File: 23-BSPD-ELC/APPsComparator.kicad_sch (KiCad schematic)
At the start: 22 parts, among them U14 LM339, U15 LM239

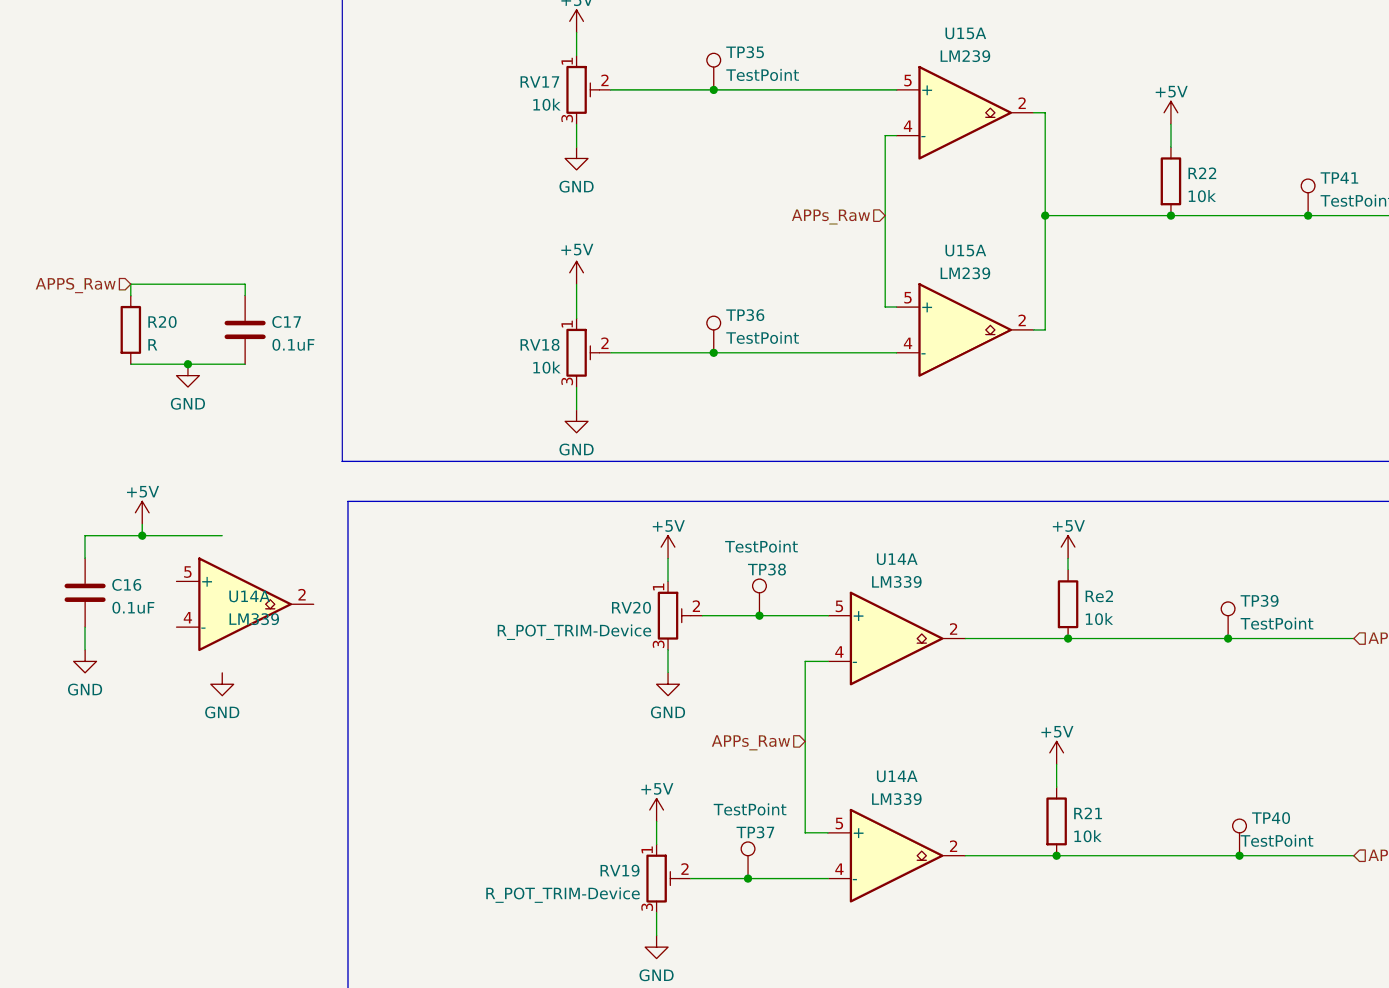
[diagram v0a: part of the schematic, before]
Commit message: Revision changes and updates to some footprints
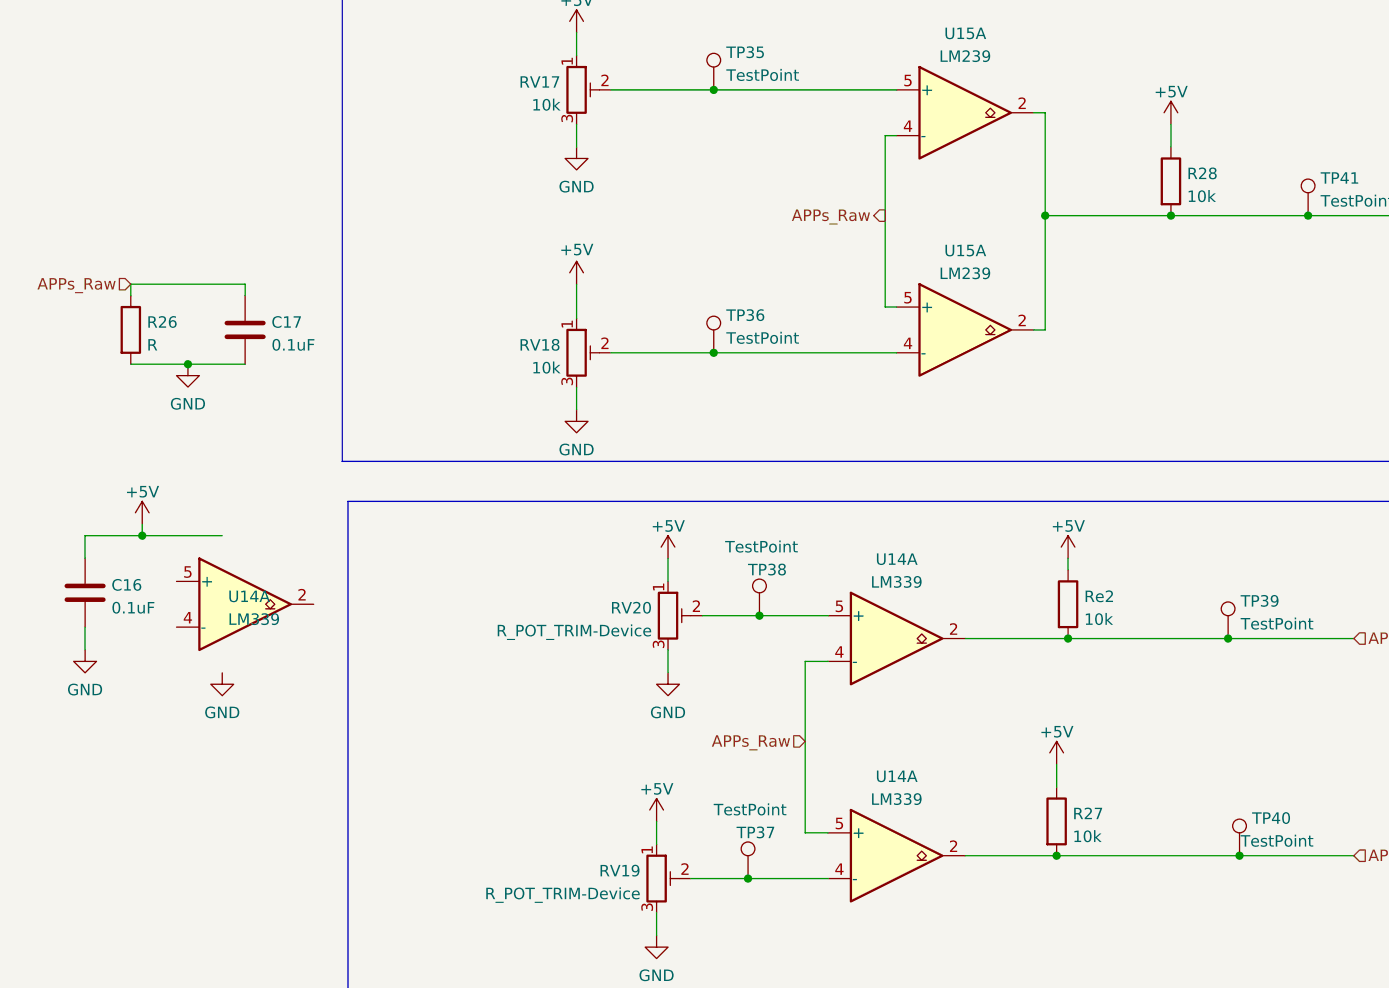
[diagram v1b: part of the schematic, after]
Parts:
- renumbered R20 to R26, R21 to R27, R22 to R28
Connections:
- net APPS_Raw is gone; now on net APPs_Raw: C17.1, R26.1
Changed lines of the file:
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@@
     (effects (font (size 1.27 1.27)) (justify left))
   )
-  (hierarchical_label "APPS_Raw" (shape input) (at 34.29 54.61 180)
+  (hierarchical_label "APPs_Raw" (shape input) (at 34.29 54.61 180)
     (effects (font (size 1.27 1.27)) (justify right))
   )
@@
     (effects (font (size 1.27 1.27)) (justify left))
   )
-  (hierarchical_label "APPs_Raw" (shape input) (at 118.11 46.99 180)
+  (hierarchical_label "APPs_Raw" (shape output) (at 118.11 46.99 180)
     (effects (font (size 1.27 1.27)) (justify right))
   )
@@
   (symbol (lib_id "power:+5V") (at 92.71 114.3 0)
     (in_bom yes) (on_board yes) (fields_autoplaced)
-    (property "Reference" "#PWR0102" (id 0) (at 92.71 118.11 0)
+    (property "Reference" "#PWR0108" (id 0) (at 92.71 118.11 0)
       (effects (font (size 1.27 1.27)) hide)
     )
@@
   (symbol (lib_id "power:GND") (at 93.98 97.79 0)
     (in_bom yes) (on_board yes) (fields_autoplaced)
-    (property "Reference" "#PWR0105" (id 0) (at 93.98 104.14 0)
+    (property "Reference" "#PWR0111" (id 0) (at 93.98 104.14 0)
       (effects (font (size 1.27 1.27)) hide)
     )
@@
   (symbol (lib_id "power:+5V") (at 83.82 54.61 0)
     (in_bom yes) (on_board yes)
-    (property "Reference" "#PWR0100" (id 0) (at 83.82 58.42 0)
+    (property "Reference" "#PWR0106" (id 0) (at 83.82 58.42 0)
       (effects (font (size 1.27 1.27)) hide)
     )
@@
   (symbol (lib_id "Device:R") (at 149.86 43.18 0)
     (in_bom yes) (on_board yes) (fields_autoplaced)
-    (property "Reference" "R22" (id 0) (at 151.638 42.3453 0)
+    (property "Reference" "R28" (id 0) (at 151.638 42.3453 0)
       (effects (font (size 1.27 1.27)) (justify left))
     )
@@
   (symbol (lib_id "power:GND") (at 29.21 95.25 0)
     (in_bom yes) (on_board yes) (fields_autoplaced)
-    (property "Reference" "#PWR094" (id 0) (at 29.21 101.6 0)
+    (property "Reference" "#PWR0100" (id 0) (at 29.21 101.6 0)
       (effects (font (size 1.27 1.27)) hide)
     )
@@
   (symbol (lib_id "power:+5V") (at 149.86 36.83 0)
     (in_bom yes) (on_board yes) (fields_autoplaced)
-    (property "Reference" "#PWR0108" (id 0) (at 149.86 40.64 0)
+    (property "Reference" "#PWR0114" (id 0) (at 149.86 40.64 0)
       (effects (font (size 1.27 1.27)) hide)
     )
@@
   (symbol (lib_id "power:+5V") (at 138.43 85.09 0)
     (in_bom yes) (on_board yes) (fields_autoplaced)
-    (property "Reference" "#PWR0107" (id 0) (at 138.43 88.9 0)
+    (property "Reference" "#PWR0113" (id 0) (at 138.43 88.9 0)
       (effects (font (size 1.27 1.27)) hide)
     )
@@
   (symbol (lib_id "power:+5V") (at 83.82 26.67 0)
     (in_bom yes) (on_board yes) (fields_autoplaced)
-    (property "Reference" "#PWR098" (id 0) (at 83.82 30.48 0)
+    (property "Reference" "#PWR0104" (id 0) (at 83.82 30.48 0)
       (effects (font (size 1.27 1.27)) hide)
     )
@@
   (symbol (lib_id "power:GND") (at 83.82 39.37 0)
     (in_bom yes) (on_board yes) (fields_autoplaced)
-    (property "Reference" "#PWR099" (id 0) (at 83.82 45.72 0)
+    (property "Reference" "#PWR0105" (id 0) (at 83.82 45.72 0)
       (effects (font (size 1.27 1.27)) hide)
     )
@@
   (symbol (lib_id "Device:R") (at 137.16 114.3 0)
     (in_bom yes) (on_board yes) (fields_autoplaced)
-    (property "Reference" "R21" (id 0) (at 138.938 113.4653 0)
+    (property "Reference" "R27" (id 0) (at 138.938 113.4653 0)
       (effects (font (size 1.27 1.27)) (justify left))
     )
@@
   (symbol (lib_id "power:GND") (at 44.45 97.79 0)
     (in_bom yes) (on_board yes) (fields_autoplaced)
-    (property "Reference" "#PWR097" (id 0) (at 44.45 104.14 0)
+    (property "Reference" "#PWR0103" (id 0) (at 44.45 104.14 0)
       (effects (font (size 1.27 1.27)) hide)
     )
@@
   (symbol (lib_id "power:GND") (at 40.64 63.5 0)
     (in_bom yes) (on_board yes) (fields_autoplaced)
-    (property "Reference" "#PWR096" (id 0) (at 40.64 69.85 0)
+    (property "Reference" "#PWR0102" (id 0) (at 40.64 69.85 0)
       (effects (font (size 1.27 1.27)) hide)
     )
@@
   (symbol (lib_id "power:+5V") (at 93.98 85.09 0)
     (in_bom yes) (on_board yes) (fields_autoplaced)
-    (property "Reference" "#PWR0104" (id 0) (at 93.98 88.9 0)
+    (property "Reference" "#PWR0110" (id 0) (at 93.98 88.9 0)
       (effects (font (size 1.27 1.27)) hide)
     )
@@
   (symbol (lib_id "power:+5V") (at 35.56 81.28 0)
     (in_bom yes) (on_board yes) (fields_autoplaced)
-    (property "Reference" "#PWR095" (id 0) (at 35.56 85.09 0)
+    (property "Reference" "#PWR0101" (id 0) (at 35.56 85.09 0)
       (effects (font (size 1.27 1.27)) hide)
     )
@@
   (symbol (lib_id "power:+5V") (at 137.16 107.95 0)
     (in_bom yes) (on_board yes) (fields_autoplaced)
-    (property "Reference" "#PWR0106" (id 0) (at 137.16 111.76 0)
+    (property "Reference" "#PWR0112" (id 0) (at 137.16 111.76 0)
       (effects (font (size 1.27 1.27)) hide)
     )
@@
   (symbol (lib_id "power:GND") (at 83.82 68.58 0)
     (in_bom yes) (on_board yes) (fields_autoplaced)
-    (property "Reference" "#PWR0101" (id 0) (at 83.82 74.93 0)
+    (property "Reference" "#PWR0107" (id 0) (at 83.82 74.93 0)
       (effects (font (size 1.27 1.27)) hide)
     )
@@
   (symbol (lib_id "Device:R") (at 34.29 59.69 0)
     (in_bom yes) (on_board yes) (fields_autoplaced)
-    (property "Reference" "R20" (id 0) (at 36.068 58.8553 0)
+    (property "Reference" "R26" (id 0) (at 36.068 58.8553 0)
       (effects (font (size 1.27 1.27)) (justify left))
     )
@@
   (symbol (lib_id "power:GND") (at 92.71 127 0)
     (in_bom yes) (on_board yes) (fields_autoplaced)
-    (property "Reference" "#PWR0103" (id 0) (at 92.71 133.35 0)
-      (effects (font (size 1.27 1.27)) hide)
-    )
+    (property "Reference" "#PWR0109" (id 0) (at 92.71 133.35 0)
+      (effects (font (size 1.27 1.27)) hide)
+    )

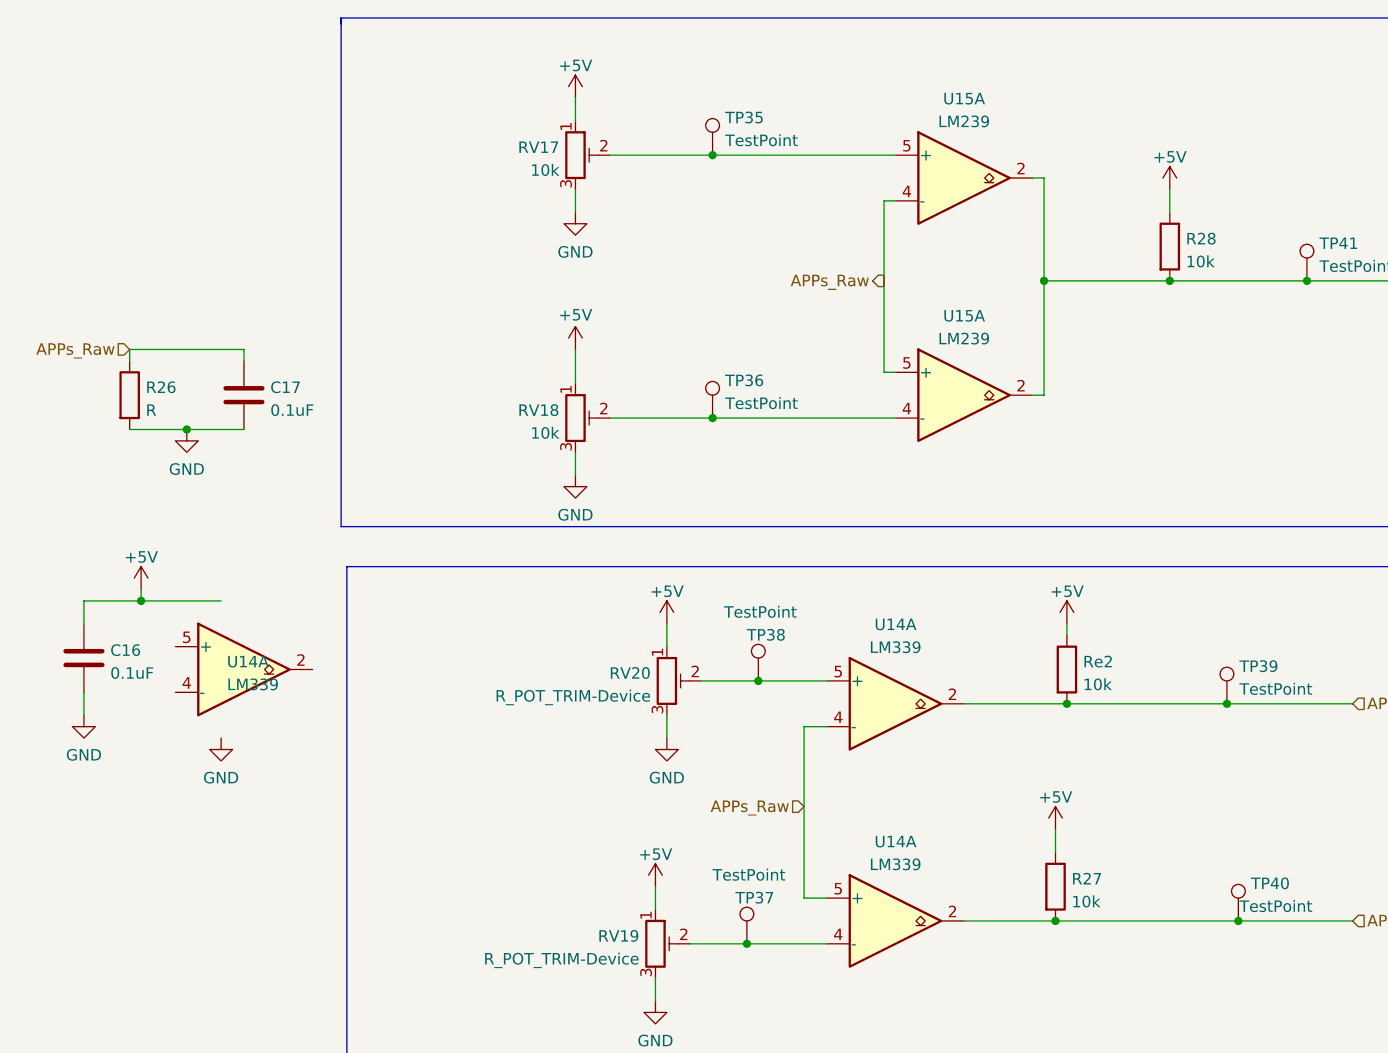
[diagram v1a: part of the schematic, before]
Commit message: Updated pcb layout; Watchdog on board still in progress
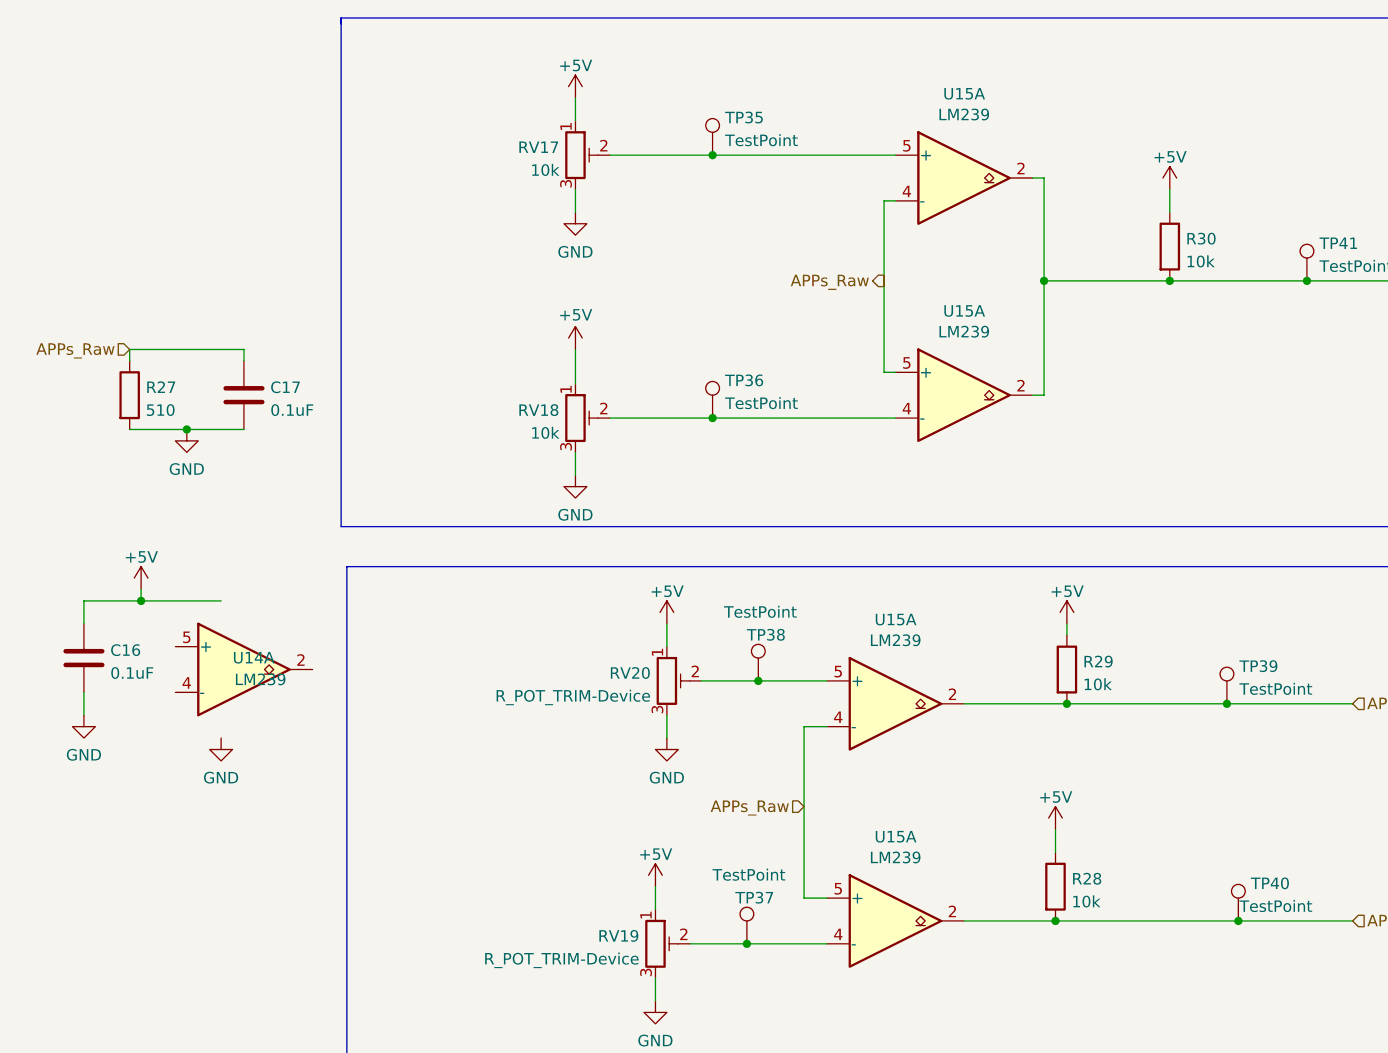
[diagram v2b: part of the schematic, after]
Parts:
- removed U14 (x3): LM339, symbol Comparator:LM339
- removed U15 (x2): LM239, symbol Comparator:LM339
- added U14: LM239, Package_SO:SO-14_3.9x8.65mm_P1.27mm, symbol Comparator:LM339
- added U15 (x4): LM239, Package_SO:SO-14_3.9x8.65mm_P1.27mm, symbol Comparator:LM2901
- R27: renamed from R26; value R -> 510
- R29: renamed from Re2; footprint (none) -> Resistor_SMD:R_0603_1608Metric_Pad0.98x0.95mm_HandSolder
- RV17, RV18, RV19, RV20: footprint LHRE Footprint Library:PV36W201C01B00 -> Global Libraries:PVG5A
- renumbered R27 to R28, R28 to R30
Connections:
- net APPs_25%: now also U15.2
- net APPs_5%: now also U15.2
- net APPs_Connected: now also U15.2, U15.2
- net APPs_Raw: now also U15.4 (-), U15.4 (-), U15.5 (+), U15.5 (+)
- net at RV20.2, TP38.1: now also U15.5 (+)
- net at RV19.2, TP37.1: now also U15.4 (-)
- net at RV18.2, TP36.1: now also U15.4 (-)
- net at RV17.2, TP35.1: now also U15.5 (+)

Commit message: BSPD layout
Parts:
- renumbered C16 to C14, C17 to C15, R27 to R23, R28 to R24, R29 to R25, R30 to R26, RV17 to RV13, RV18 to RV14, RV19 to RV15, RV20 to RV16, TP35 to TP28, TP36 to TP29, TP37 to TP30, TP38 to TP31, TP39 to TP32, TP40 to TP33, TP41 to TP34, U15 to U13, U14 to U13
